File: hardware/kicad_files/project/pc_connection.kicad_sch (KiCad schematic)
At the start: 21 parts, among them U4 GT-USB-7010ASV, U5 FT232H

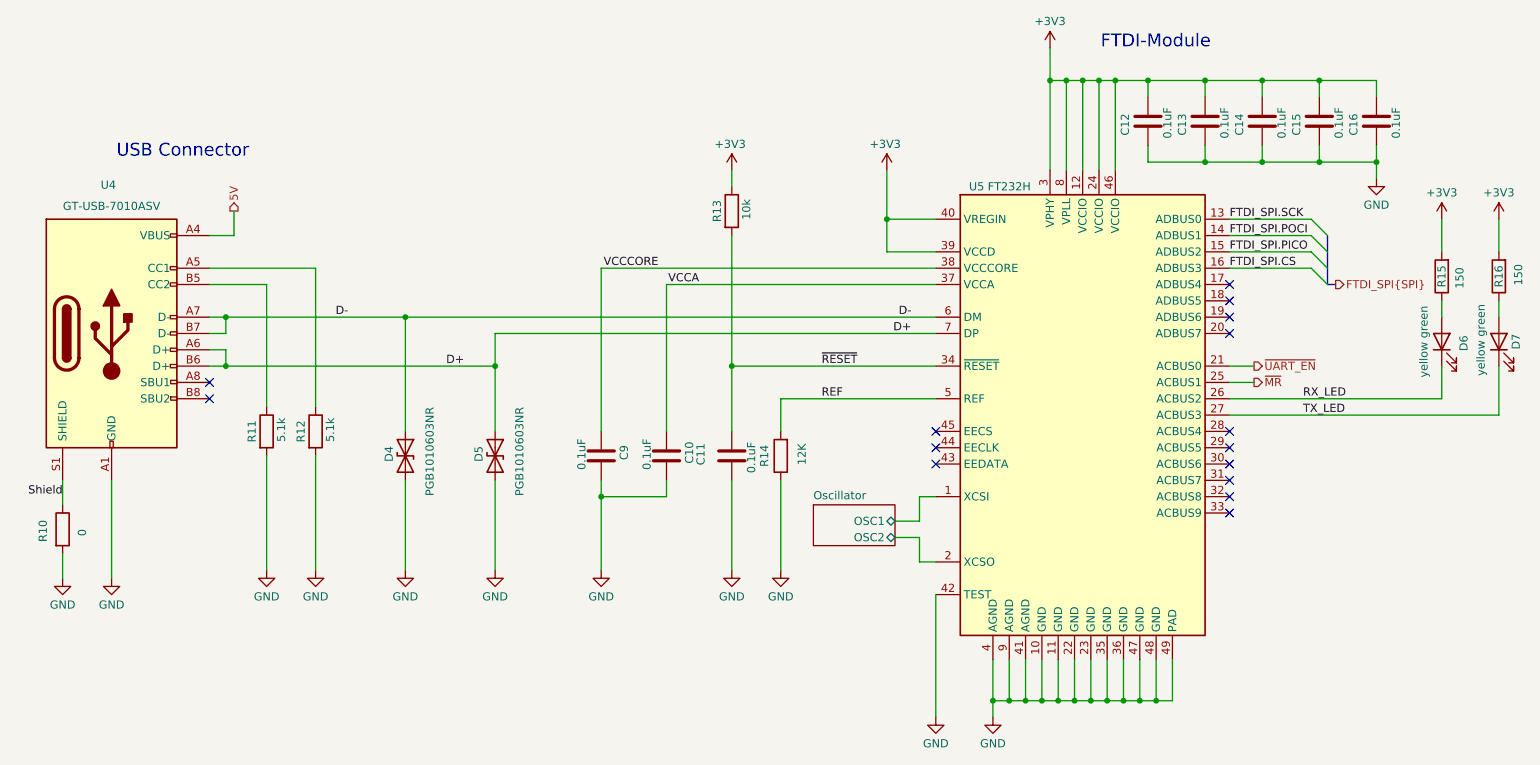
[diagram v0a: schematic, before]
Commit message: feat: update to 0.2
feat: add pin sockets compatible to the Pmod interface

feat: add a power switch and an overcurrent protection circuit, including a fault status LED and a solder bridge

fix: remove the clock jumpers and directly connect the second output clock to the user clock input

misc: remove the jumpers from io 36 and 37 to the bitbang inputs, add bitbang pins to the UART connector

cosmetic: make the PCB edges round
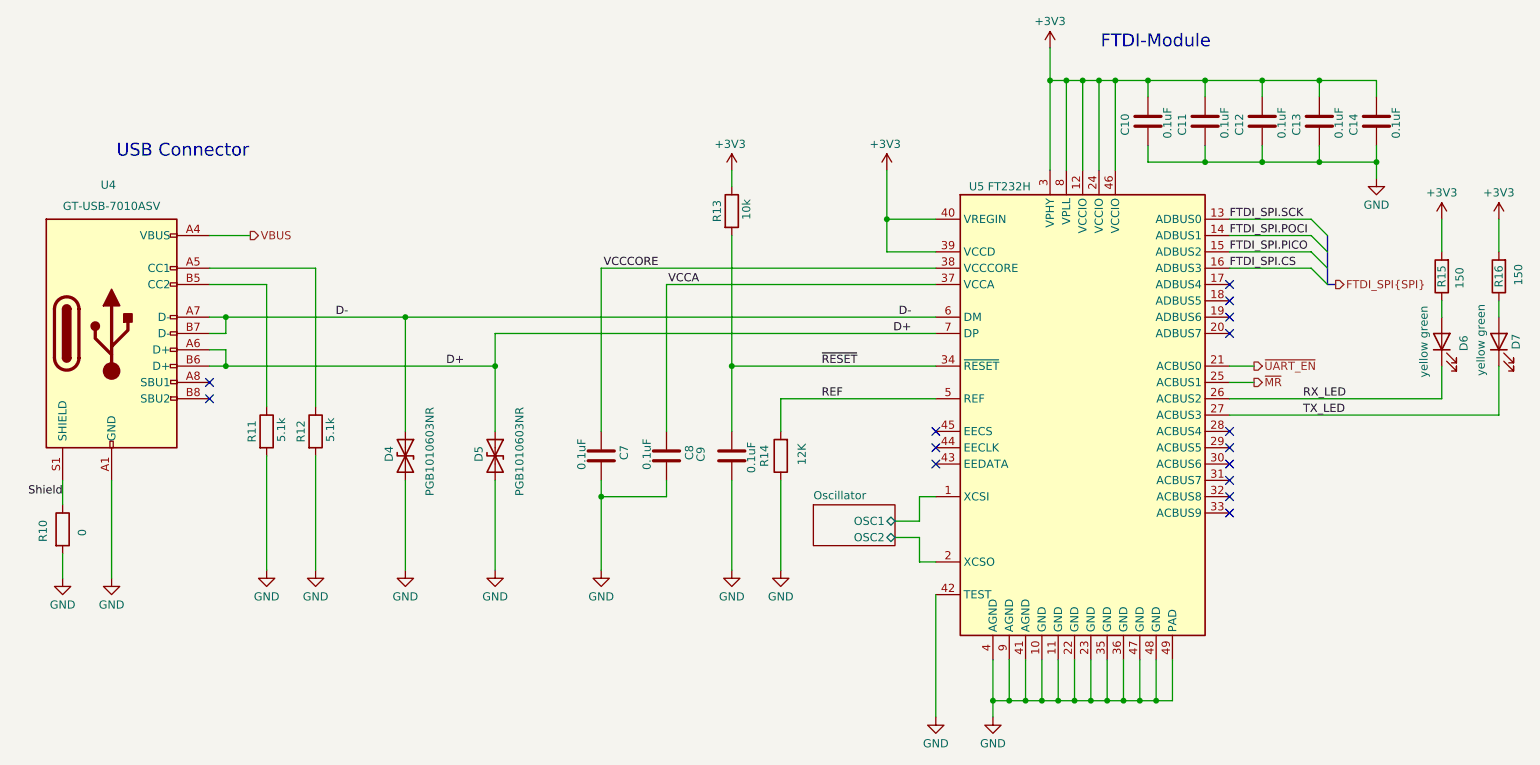
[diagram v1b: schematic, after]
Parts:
- renumbered C12 to C10, C13 to C11, C14 to C12, C15 to C13, C16 to C14, C9 to C7, C10 to C8, C11 to C9
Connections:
- net 5V renamed VBUS
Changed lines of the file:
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@@
 		(title "PC connection")
 		(date "2024-05-30")
-		(rev "0.1.1")
+		(rev "0.2.0")
 	)
 	(junction
@@
 	(wire
 		(pts
-			(xy 60.96 76.2) (xy 64.77 76.2)
+			(xy 60.96 76.2) (xy 67.31 76.2)
 		)
 		(stroke
@@
 	(wire
 		(pts
-			(xy 64.77 72.39) (xy 64.77 76.2)
-		)
-		(stroke
-			(width 0)
-			(type default)
-		)
-	)
-	(wire
-		(pts
 			(xy 203.2 148.59) (xy 200.66 148.59)
 		)
@@
 		)
 	)
-	(hierarchical_label "5V"
+	(hierarchical_label "VBUS"
 		(shape output)
-		(at 64.77 72.39 90)
+		(at 67.31 76.2 0)
 		(effects
 			(font
@@
 		(on_board yes)
 		(dnp no)
-		(property "Reference" "C11"
+		(property "Reference" "C9"
 			(at 137.414 110.236 90)
 			(effects
@@
 			(project "FABulous_board"
 				(path "/5664f05e-a3ef-4177-8026-c4580fa32c71/b4d9b251-031a-4875-8b01-0478a187070c"
-					(reference "C11")
+					(reference "C9")
 					(unit 1)
 				)
@@
 		(dnp no)
 		(fields_autoplaced yes)
-		(property "Reference" "#PWR040"
+		(property "Reference" "#PWR38"
 			(at 77.47 134.62 0)
 			(effects
@@
 			(project "FABulous_board"
 				(path "/5664f05e-a3ef-4177-8026-c4580fa32c71/b4d9b251-031a-4875-8b01-0478a187070c"
-					(reference "#PWR040")
+					(reference "#PWR38")
 					(unit 1)
 				)
@@
 		(dnp no)
 		(fields_autoplaced yes)
-		(property "Reference" "#PWR045"
+		(property "Reference" "#PWR43"
 			(at 142.24 134.62 0)
 			(effects
@@
 			(project "FABulous_board"
 				(path "/5664f05e-a3ef-4177-8026-c4580fa32c71/b4d9b251-031a-4875-8b01-0478a187070c"
-					(reference "#PWR045")
+					(reference "#PWR43")
 					(unit 1)
 				)
@@
 		(on_board yes)
 		(dnp no)
-		(property "Reference" "#PWR044"
+		(property "Reference" "#PWR42"
 			(at 142.24 69.85 0)
 			(effects
@@
 			(project "FABulous_board"
 				(path "/5664f05e-a3ef-4177-8026-c4580fa32c71/b4d9b251-031a-4875-8b01-0478a187070c"
-					(reference "#PWR044")
+					(reference "#PWR42")
 					(unit 1)
 				)
@@
 		(dnp no)
 		(fields_autoplaced yes)
-		(property "Reference" "#PWR042"
+		(property "Reference" "#PWR40"
 			(at 105.41 134.62 0)
 			(effects
@@
 			(project "FABulous_board"
 				(path "/5664f05e-a3ef-4177-8026-c4580fa32c71/b4d9b251-031a-4875-8b01-0478a187070c"
-					(reference "#PWR042")
+					(reference "#PWR40")
 					(unit 1)
 				)
@@
 		(dnp no)
 		(fields_autoplaced yes)
-		(property "Reference" "#PWR041"
+		(property "Reference" "#PWR39"
 			(at 91.44 134.62 0)
 			(effects
@@
 			(project "FABulous_board"
 				(path "/5664f05e-a3ef-4177-8026-c4580fa32c71/b4d9b251-031a-4875-8b01-0478a187070c"
-					(reference "#PWR041")
+					(reference "#PWR39")
 					(unit 1)
 				)
@@
 		(dnp no)
 		(fields_autoplaced yes)
-		(property "Reference" "#PWR043"
+		(property "Reference" "#PWR41"
 			(at 121.92 134.62 0)
 			(effects
@@
 			(project "FABulous_board"
 				(path "/5664f05e-a3ef-4177-8026-c4580fa32c71/b4d9b251-031a-4875-8b01-0478a187070c"
-					(reference "#PWR043")
+					(reference "#PWR41")
 					(unit 1)
 				)
@@
 		(dnp no)
 		(fields_autoplaced yes)
-		(property "Reference" "#PWR052"
+		(property "Reference" "#PWR50"
 			(at 252.73 77.47 0)
 			(effects
@@
 			(project "FABulous_board"
 				(path "/5664f05e-a3ef-4177-8026-c4580fa32c71/b4d9b251-031a-4875-8b01-0478a187070c"
-					(reference "#PWR052")
+					(reference "#PWR50")
 					(unit 1)
 				)
@@
 		(on_board yes)
 		(dnp no)
-		(property "Reference" "C9"
+		(property "Reference" "C7"
 			(at 125.476 109.982 90)
 			(effects
@@
 			(project "FABulous_board"
 				(path "/5664f05e-a3ef-4177-8026-c4580fa32c71/b4d9b251-031a-4875-8b01-0478a187070c"
-					(reference "C9")
+					(reference "C7")
 					(unit 1)
 				)
@@
 		(dnp no)
 		(fields_autoplaced yes)
-		(property "Reference" "#PWR039"
+		(property "Reference" "#PWR37"
 			(at 69.85 134.62 0)
 			(effects
@@
 			(project "FABulous_board"
 				(path "/5664f05e-a3ef-4177-8026-c4580fa32c71/b4d9b251-031a-4875-8b01-0478a187070c"
-					(reference "#PWR039")
+					(reference "#PWR37")
 					(unit 1)
 				)
@@
 		(dnp no)
 		(fields_autoplaced yes)
-		(property "Reference" "#PWR049"
+		(property "Reference" "#PWR47"
 			(at 182.88 157.48 0)
 			(effects
@@
 			(project "FABulous_board"
 				(path "/5664f05e-a3ef-4177-8026-c4580fa32c71/b4d9b251-031a-4875-8b01-0478a187070c"
-					(reference "#PWR049")
+					(reference "#PWR47")
 					(unit 1)
 				)
@@
 		(on_board yes)
 		(dnp no)
-		(property "Reference" "C10"
+		(property "Reference" "C8"
 			(at 135.636 109.982 90)
 			(effects
@@
 			(project "FABulous_board"
 				(path "/5664f05e-a3ef-4177-8026-c4580fa32c71/b4d9b251-031a-4875-8b01-0478a187070c"
-					(reference "C10")
+					(reference "C8")
 					(unit 1)
 				)
@@
 		(on_board yes)
 		(dnp no)
-		(property "Reference" "#PWR047"
+		(property "Reference" "#PWR45"
 			(at 166.37 69.85 0)
 			(effects
@@
 			(project "FABulous_board"
 				(path "/5664f05e-a3ef-4177-8026-c4580fa32c71/b4d9b251-031a-4875-8b01-0478a187070c"
-					(reference "#PWR047")
+					(reference "#PWR45")
 					(unit 1)
 				)
@@
 		(dnp no)
 		(fields_autoplaced yes)
-		(property "Reference" "#PWR048"
+		(property "Reference" "#PWR46"
 			(at 173.99 157.48 0)
 			(effects
@@
 			(project "FABulous_board"
 				(path "/5664f05e-a3ef-4177-8026-c4580fa32c71/b4d9b251-031a-4875-8b01-0478a187070c"
-					(reference "#PWR048")
+					(reference "#PWR46")
 					(unit 1)
 				)
@@
 		(dnp no)
 		(fields_autoplaced yes)
-		(property "Reference" "#PWR051"
+		(property "Reference" "#PWR49"
 			(at 242.57 73.66 0)
 			(effects
@@
 			(project "FABulous_board"
 				(path "/5664f05e-a3ef-4177-8026-c4580fa32c71/b4d9b251-031a-4875-8b01-0478a187070c"
-					(reference "#PWR051")
+					(reference "#PWR49")
 					(unit 1)
 				)
@@
 		(on_board yes)
 		(dnp no)
-		(property "Reference" "C16"
+		(property "Reference" "C14"
 			(at 239.014 58.928 90)
 			(effects
@@
 			(project "FABulous_board"
 				(path "/5664f05e-a3ef-4177-8026-c4580fa32c71/b4d9b251-031a-4875-8b01-0478a187070c"
-					(reference "C16")
+					(reference "C14")
 					(unit 1)
 				)
@@
 		(on_board yes)
 		(dnp no)
-		(property "Reference" "C14"
+		(property "Reference" "C12"
 			(at 221.234 58.928 90)
 			(effects
@@
 			(project "FABulous_board"
 				(path "/5664f05e-a3ef-4177-8026-c4580fa32c71/b4d9b251-031a-4875-8b01-0478a187070c"
-					(reference "C14")
+					(reference "C12")
 					(unit 1)
 				)
@@
 		(dnp no)
 		(fields_autoplaced yes)
-		(property "Reference" "#PWR050"
+		(property "Reference" "#PWR48"
 			(at 191.77 50.8 0)
 			(effects
@@
 			(project "FABulous_board"
 				(path "/5664f05e-a3ef-4177-8026-c4580fa32c71/b4d9b251-031a-4875-8b01-0478a187070c"
-					(reference "#PWR050")
+					(reference "#PWR48")
 					(unit 1)
 				)
@@
 		(dnp no)
 		(fields_autoplaced yes)
-		(property "Reference" "#PWR046"
+		(property "Reference" "#PWR44"
 			(at 149.86 134.62 0)
 			(effects
@@
 			(project "FABulous_board"
 				(path "/5664f05e-a3ef-4177-8026-c4580fa32c71/b4d9b251-031a-4875-8b01-0478a187070c"
-					(reference "#PWR046")
+					(reference "#PWR44")
 					(unit 1)
 				)
@@
 		(on_board yes)
 		(dnp no)
-		(property "Reference" "C12"
+		(property "Reference" "C10"
 			(at 203.454 58.928 90)
 			(effects
@@
 			(project "FABulous_board"
 				(path "/5664f05e-a3ef-4177-8026-c4580fa32c71/b4d9b251-031a-4875-8b01-0478a187070c"
-					(reference "C12")
+					(reference "C10")
 					(unit 1)
 				)
@@
 		(on_board yes)
 		(dnp no)
-		(property "Reference" "C15"
+		(property "Reference" "C13"
 			(at 230.124 58.928 90)
 			(effects
@@
 			(project "FABulous_board"
 				(path "/5664f05e-a3ef-4177-8026-c4580fa32c71/b4d9b251-031a-4875-8b01-0478a187070c"
-					(reference "C15")
+					(reference "C13")
 					(unit 1)
 				)
@@
 		(dnp no)
 		(fields_autoplaced yes)
-		(property "Reference" "#PWR037"
+		(property "Reference" "#PWR36"
 			(at 45.72 135.89 0)
 			(effects
@@
 			(project "FABulous_board"
 				(path "/5664f05e-a3ef-4177-8026-c4580fa32c71/b4d9b251-031a-4875-8b01-0478a187070c"
-					(reference "#PWR037")
+					(reference "#PWR36")
 					(unit 1)
 				)
@@
 		(dnp no)
 		(fields_autoplaced yes)
-		(property "Reference" "#PWR053"
+		(property "Reference" "#PWR51"
 			(at 261.62 77.47 0)
 			(effects
@@
 			(project "FABulous_board"
 				(path "/5664f05e-a3ef-4177-8026-c4580fa32c71/b4d9b251-031a-4875-8b01-0478a187070c"
-					(reference "#PWR053")
+					(reference "#PWR51")
 					(unit 1)
 				)
@@
 		(dnp no)
 		(fields_autoplaced yes)
-		(property "Reference" "#PWR036"
+		(property "Reference" "#PWR35"
 			(at 38.1 135.89 0)
 			(effects
@@
 			(project "FABulous_board"
 				(path "/5664f05e-a3ef-4177-8026-c4580fa32c71/b4d9b251-031a-4875-8b01-0478a187070c"
-					(reference "#PWR036")
+					(reference "#PWR35")
 					(unit 1)
 				)
@@
 		(on_board yes)
 		(dnp no)
-		(property "Reference" "C13"
+		(property "Reference" "C11"
 			(at 212.344 58.928 90)
 			(effects
@@
 			(project "FABulous_board"
 				(path "/5664f05e-a3ef-4177-8026-c4580fa32c71/b4d9b251-031a-4875-8b01-0478a187070c"
-					(reference "C13")
+					(reference "C11")
 					(unit 1)
 				)
